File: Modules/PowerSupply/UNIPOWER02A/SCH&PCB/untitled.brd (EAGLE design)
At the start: 40.1 x 40.1 mm, 20 parts, among them X1 WAGO256, X2 WAGO256, X3 WAGO256, X4 M3, X5 M3, X6 M3, X7 M3, X8 WAGO256, X9 DC 2.1MM

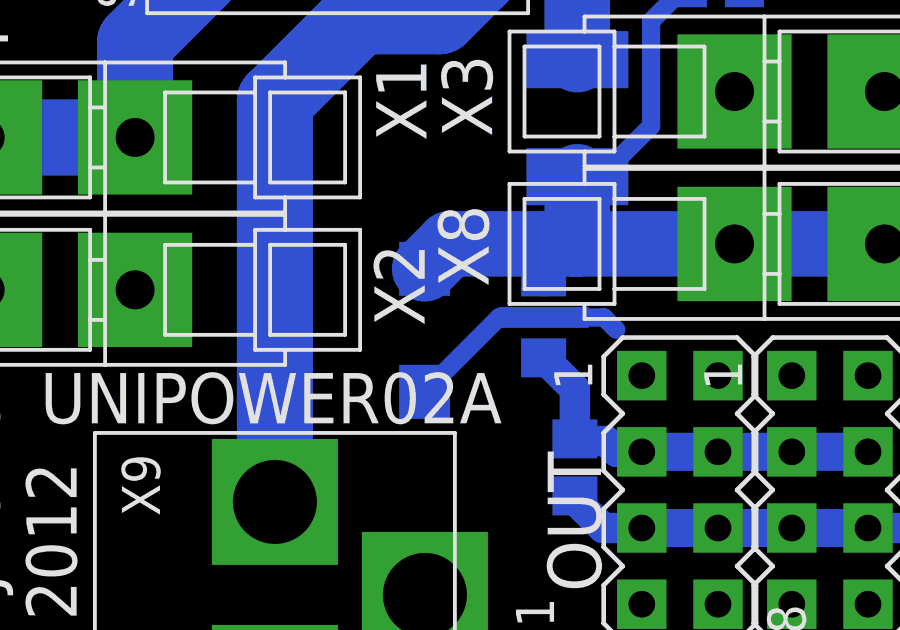
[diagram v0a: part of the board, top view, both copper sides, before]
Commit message: 
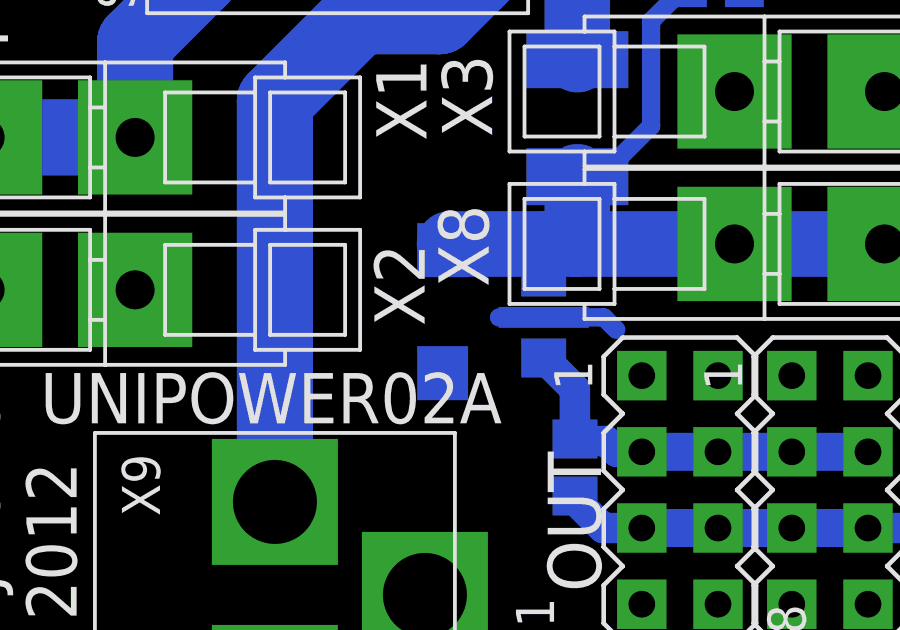
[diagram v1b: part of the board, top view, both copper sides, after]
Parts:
- moved D4 0.86 mm to (20.6, 20.3), turned to 90 degrees
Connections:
- net GND12: now also D4.A; no longer D4.K
- net N$9: now also D4.K; no longer D4.A
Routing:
- net GND12: track 8.09 -> 4.58 mm
- net N$9: track 27.4 -> 26.3 mm
